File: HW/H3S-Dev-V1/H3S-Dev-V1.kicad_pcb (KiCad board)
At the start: 2 copper layers, 85 x 56 mm, 33 parts, among them J1 USB_C_Receptacle_USB2.0_16P, J2 Conn_01x02_Socket, J3 Conn_Coaxial, Q1 DMP3099L, U1 Ai-Thinker-Ra-01, U2 LTC4054ES5-4.2, U3 USBLC6-2SC6, U4 ESP32-S3-WROOM-1, U5 SY8089AAAC

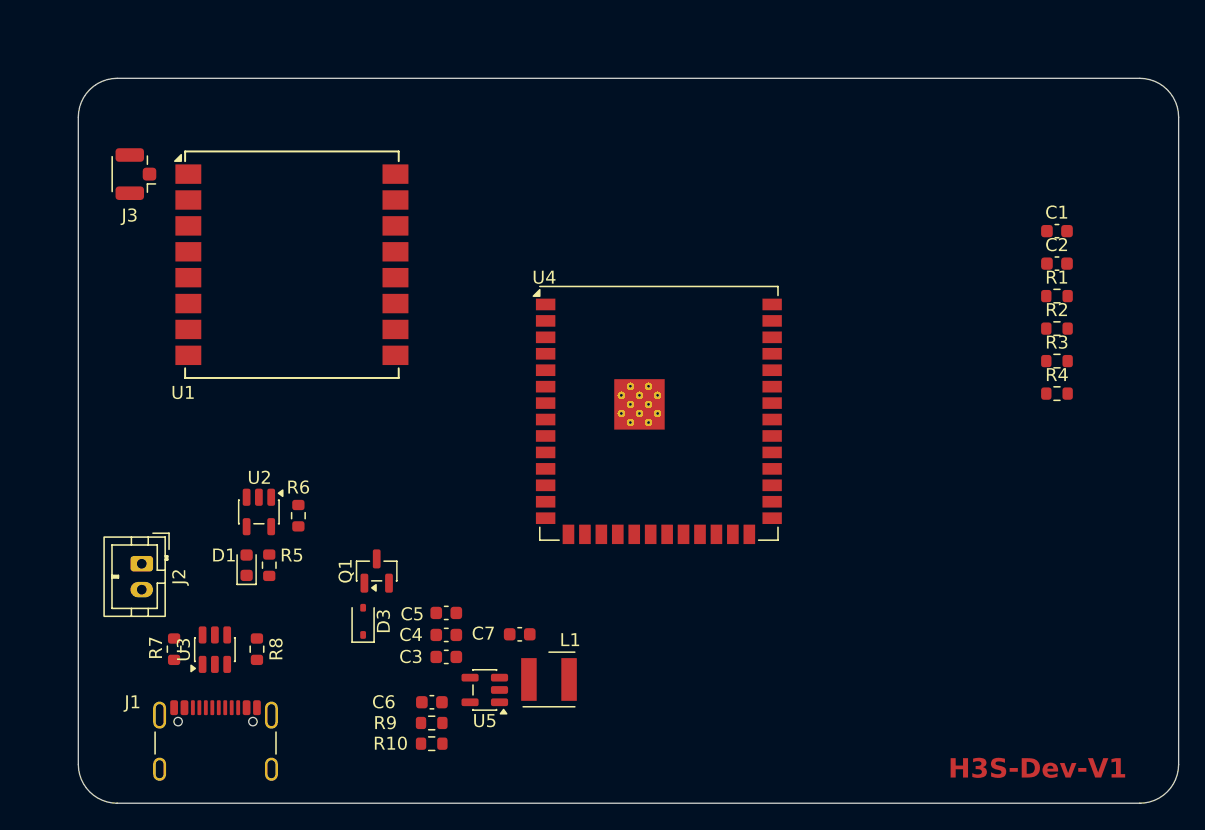
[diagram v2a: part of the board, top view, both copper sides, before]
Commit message: PCB dimensions
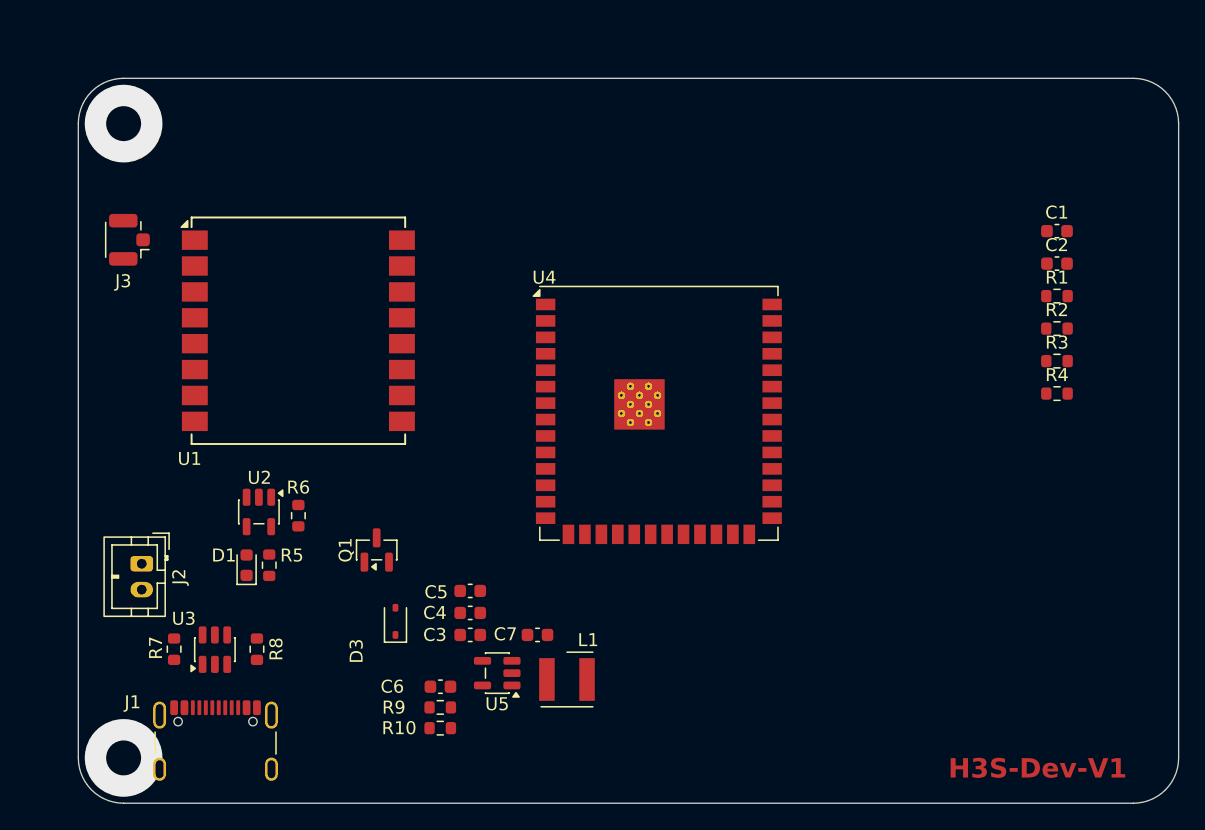
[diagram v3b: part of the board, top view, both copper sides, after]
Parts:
- moved U1 5.12 mm to (117.0, 93.5)
- moved J3 5.10 mm to (104.0, 86.5)
- moved C3 2.51 mm to (130.3, 117.0)
- moved C4 2.51 mm to (130.3, 115.3)
- moved C5 2.51 mm to (130.3, 113.6)
- moved D3 2.50 mm to (124.5, 116.0)
- moved Q1 1.62 mm to (123.0, 110.4)
- moved U5 1.62 mm to (132.4, 120.0)
- moved L1 1.39 mm to (137.8, 120.4)
- moved C7 1.38 mm to (135.5, 117.0)
- moved C6 1.37 mm to (128.0, 121.0)
- moved R10 1.37 mm to (128.0, 124.2)
- moved R9 1.37 mm to (128.0, 122.6)
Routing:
- net GND: vias 0 -> 2
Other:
- outline, holes or cut-outs redrawn
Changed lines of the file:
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@@
 	(footprint "Connector_Coaxial:U.FL_Hirose_U.FL-R-SMT-1_Vertical"
 		(layer "F.Cu")
-		(at 104.45 81.4 180)
+		(at 103.95 86.475 180)
 		(descr "Hirose U.FL Coaxial https://www.hirose.com/product/en/products/U.FL/U.FL-R-SMT-1%2810%29/")
 		(tags "Hirose U.FL Coaxial")
@@
 			(polygon
 				(pts
-					(xy 102.875 82.35) (xy 104.965 82.35) (xy 104.965 80.45) (xy 102.875 80.45)
+					(xy 102.375 87.425) (xy 104.465 87.425) (xy 104.465 85.525) (xy 102.375 85.525)
 				)
 			)
@@
 	(footprint "Capacitor_SMD:C_0603_1608Metric"
 		(layer "F.Cu")
-		(at 127.315 122.2)
+		(at 127.975 121)
 		(descr "Capacitor SMD 0603 (1608 Metric), square (rectangular) end terminal, IPC-7351 nominal, (Body size source: IPC-SM-782 page 76, https://www.pcb-3d.com/wordpress/wp-content/uploads/ipc-sm-782a_amendment_1_and_2.pdf), generated with kicad-footprint-generator")
 		(tags "capacitor")
@@
 	(footprint "Resistor_SMD:R_0603_1608Metric"
 		(layer "F.Cu")
-		(at 127.3 123.8)
+		(at 127.96 122.6)
 		(descr "Resistor SMD 0603 (1608 Metric), square (rectangular) end terminal, IPC-7351 nominal, (Body size source: IPC-SM-782 page 72, https://www.pcb-3d.com/wordpress/wp-content/uploads/ipc-sm-782a_amendment_1_and_2.pdf), generated with kicad-footprint-generator")
 		(tags "resistor")
@@
 	(footprint "Package_TO_SOT_SMD:SOT-23"
 		(layer "F.Cu")
-		(at 123.05 112.0625 90)
+		(at 123.05 110.4375 90)
 		(descr "SOT, 3 Pin (JEDEC TO-236 Var AB https://www.jedec.org/document_search?search_api_views_fulltext=TO-236), generated with kicad-footprint-generator ipc_gullwing_generator.py")
 		(tags "SOT TO_SOT_SMD")
@@
 	(footprint "Capacitor_SMD:C_0603_1608Metric"
 		(layer "F.Cu")
-		(at 128.425 115.3)
+		(at 130.275 113.6)
 		(descr "Capacitor SMD 0603 (1608 Metric), square (rectangular) end terminal, IPC-7351 nominal, (Body size source: IPC-SM-782 page 76, https://www.pcb-3d.com/wordpress/wp-content/uploads/ipc-sm-782a_amendment_1_and_2.pdf), generated with kicad-footprint-generator")
 		(tags "capacitor")
@@
 	(footprint "Inductor_SMD_Wurth:L_Wurth_WE-LQSH-4020"
 		(layer "F.Cu")
-		(at 136.36 120.44)
+		(at 137.75 120.44)
 		(descr "Semi-Shielded High Saturation Power Inductor, body 4x4mm, https://www.we-online.com/catalog/en/WE-LQSH#/articles/WE-LQSH-4020")
 		(tags "SMT")
@@
 	(footprint "Package_TO_SOT_SMD:SOT-23-5"
 		(layer "F.Cu")
-		(at 131.4 121.25 180)
+		(at 132.3625 119.95 180)
 		(descr "SOT, 5 Pin (JEDEC MO-178 Var AA https://www.jedec.org/document_search?search_api_views_fulltext=MO-178), generated with kicad-footprint-generator ipc_gullwing_generator.py")
 		(tags "SOT TO_SOT_SMD")
@@
 	(footprint "Diode_SMD:D_SOD-323"
 		(layer "F.Cu")
-		(at 122 115.95 90)
+		(at 124.5 115.95 90)
 		(descr "SOD-323")
 		(tags "SOD-323")
 		(property "Reference" "D3"
-			(at 0 1.6 90)
+			(at -2.3 -3 90)
 			(layer "F.SilkS")
 			(effects
@@
 		)
 		(fp_text user "${REFERENCE}"
-			(at 0 -1.85 90)
+			(at 0 -1.75 90)
 			(layer "F.Fab")
 			(effects
@@
 	(footprint "Capacitor_SMD:C_0603_1608Metric"
 		(layer "F.Cu")
-		(at 128.425 118.7)
+		(at 130.275 117)
 		(descr "Capacitor SMD 0603 (1608 Metric), square (rectangular) end terminal, IPC-7351 nominal, (Body size source: IPC-SM-782 page 76, https://www.pcb-3d.com/wordpress/wp-content/uploads/ipc-sm-782a_amendment_1_and_2.pdf), generated with kicad-footprint-generator")
 		(tags "capacitor")
@@
 	(footprint "RF_Module:Ai-Thinker-Ra-01-LoRa"
 		(layer "F.Cu")
-		(at 116.5 88.4)
+		(at 117 93.5)
 		(descr "Ai Thinker Ra-01 LoRa")
 		(tags "LoRa Ra-01")
@@
 	(footprint "Capacitor_SMD:C_0603_1608Metric"
 		(layer "F.Cu")
-		(at 134.1 116.95 180)
+		(at 135.475 117 180)
 		(descr "Capacitor SMD 0603 (1608 Metric), square (rectangular) end terminal, IPC-7351 nominal, (Body size source: IPC-SM-782 page 76, https://www.pcb-3d.com/wordpress/wp-content/uploads/ipc-sm-782a_amendment_1_and_2.pdf), generated with kicad-footprint-generator")
 		(tags "capacitor")
 		(property "Reference" "C7"
-			(at 2.8 0.05 0)
+			(at 2.475 0.05 0)
 			(layer "F.SilkS")
 			(effects
@@
 		(tags "SOT TO_SOT_SMD")
 		(property "Reference" "U3"
-			(at 0 -2.4 90)
+			(at 2.3875 -2.4 180)
 			(layer "F.SilkS")
 			(effects
@@
 	(footprint "Capacitor_SMD:C_0603_1608Metric"
 		(layer "F.Cu")
-		(at 128.425 117)
+		(at 130.275 115.3)
 		(descr "Capacitor SMD 0603 (1608 Metric), square (rectangular) end terminal, IPC-7351 nominal, (Body size source: IPC-SM-782 page 76, https://www.pcb-3d.com/wordpress/wp-content/uploads/ipc-sm-782a_amendment_1_and_2.pdf), generated with kicad-footprint-generator")
 		(tags "capacitor")
@@
 	(footprint "Resistor_SMD:R_0603_1608Metric"
 		(layer "F.Cu")
-		(at 127.3 125.4 180)
+		(at 127.96 124.2 180)
 		(descr "Resistor SMD 0603 (1608 Metric), square (rectangular) end terminal, IPC-7351 nominal, (Body size source: IPC-SM-782 page 72, https://www.pcb-3d.com/wordpress/wp-content/uploads/ipc-sm-782a_amendment_1_and_2.pdf), generated with kicad-footprint-generator")
 		(tags "resistor")
@@
 	)
 	(gr_arc
-		(start 103 130)
-		(mid 100.87868 129.12132)
-		(end 100 127)
+		(start 100 77.5)
+		(mid 101.025126 75.025126)
+		(end 103.5 74)
 		(stroke
-			(width 0.05)
-			(type default)
+			(width 0.1)
+			(type solid)
 		)
 		(locked yes)
 		(layer "Edge.Cuts")
 	)
-	(gr_arc
-		(start 185 127)
-		(mid 184.12132 129.12132)
-		(end 182 130)
+	(gr_line
+		(start 181.5 74)
+		(end 103.5 74)
 		(stroke
-			(width 0.05)
-			(type default)
+			(width 0.1)
+			(type solid)
 		)
 		(locked yes)
@@
 	)
 	(gr_line
-		(start 185 77)
-		(end 185 127)
+		(start 103.5 130)
+		(end 181.5 130)
 		(stroke
-			(width 0.05)
-			(type default)
+			(width 0.1)
+			(type solid)
 		)
 		(locked yes)
 		(layer "Edge.Cuts")
 	)
-	(gr_line
-		(start 103 130)
-		(end 182 130)
+	(gr_arc
+		(start 103.5 130)
+		(mid 101.025126 128.974874)
+		(end 100 126.5)
 		(stroke
-			(width 0.05)
-			(type default)
+			(width 0.1)
+			(type solid)
 		)
 		(locked yes)
 		(layer "Edge.Cuts")
 	)
-	(gr_arc
-		(start 182 74)
-		(mid 184.12132 74.87868)
-		(end 185 77)
+	(gr_line
+		(start 100 77.5)
+		(end 100 126.5)
 		(stroke
-			(width 0.05)
-			(type default)
+			(width 0.1)
+			(type solid)
 		)
 		(locked yes)
 		(layer "Edge.Cuts")
 	)
-	(gr_line
-		(start 100 77)
-		(end 100 127)
+	(gr_arc
+		(start 185 126.5)
+		(mid 183.974874 128.974874)
+		(end 181.5 130)
 		(stroke
-			(width 0.05)
-			(type default)
+			(width 0.1)
+			(type solid)
 		)
 		(locked yes)
@@
 	)
 	(gr_line
-		(start 103 74)
-		(end 182 74)
+		(start 185 126.5)
+		(end 185 77.5)
 		(stroke
-			(width 0.05)
-			(type default)
+			(width 0.1)
+			(type solid)
 		)
 		(locked yes)
@@
 	)
 	(gr_arc
-		(start 100 77)
-		(mid 100.87868 74.87868)
-		(end 103 74)
+		(start 181.5 74)
+		(mid 183.974874 75.025126)
+		(end 185 77.5)
 		(stroke
-			(width 0.05)
-			(type default)
+			(width 0.1)
+			(type solid)
 		)
 		(locked yes)
 		(layer "Edge.Cuts")
 	)
-	(gr_arc
-		(start 185 127)
-		(mid 184.12132 129.12132)
-		(end 182 130)
+	(gr_line
+		(start 100.000001 126.5)
+		(end 100.000001 77.499999)
 		(stroke
-			(width 0.5)
+			(width 1)
 			(type solid)
 		)
@@
 		(layer "Margin")
 	)
-	(gr_line
-		(start 103 130)
-		(end 182 130)
+	(gr_arc
+		(start 100.000001 77.5)
+		(mid 101.025127 75.025126)
+		(end 103.500001 74)
 		(stroke
-			(width 0.5)
+			(width 1)
 			(type solid)
 		)
@@
 		(layer "Margin")
 	)
-	(gr_line
-		(start 100 77)
-		(end 100 127)
+	(gr_arc
+		(start 103.5 130)
+		(mid 101.025126 128.974874)
+		(end 100 126.5)
 		(stroke
-			(width 0.5)
+			(width 1)
 			(type solid)
 		)
@@
 	)
 	(gr_arc
-		(start 100 77)
-		(mid 100.87868 74.87868)
-		(end 103 74)
+		(start 181.500001 74.000001)
+		(mid 183.974875 75.025127)
+		(end 185.000001 77.500001)
 		(stroke
-			(width 0.5)
+			(width 1)
 			(type solid)
 		)
@@
 	)
 	(gr_line
-		(start 103 74)
-		(end 182 74)
+		(start 103.5 130)
+		(end 181.5 130)
 		(stroke
-			(width 0.5)
+			(width 1)
 			(type solid)
 		)
@@
 		(layer "Margin")
 	)
-	(gr_arc
-		(start 103 130)
-		(mid 100.87868 129.12132)
-		(end 100 127)
+	(gr_line
+		(start 184.999999 126.500002)
+		(end 184.999999 77.500001)
 		(stroke
-			(width 0.5)
+			(width 1)
 			(type solid)
 		)
@@
 	)
 	(gr_arc
-		(start 182 74)
-		(mid 184.12132 74.87868)
-		(end 185 77)
+		(start 184.999999 126.499999)
+		(mid 183.974873 128.974873)
+		(end 181.499999 129.999999)
 		(stroke
-			(width 0.5)
+			(width 1)
 			(type solid)
 		)
@@
 	)
 	(gr_line
-		(start 185 77)
-		(end 185 127)
+		(start 103.5 74)
+		(end 181.5 74)
 		(stroke
-			(width 0.5)
+			(width 1)
 			(type solid)
 		)
@@
 		)
 	)
+	(via
+		(at 103.5 126.5)
+		(size 6)
+		(drill 2.7)
+		(layers "F.Cu" "B.Cu")
+		(net 2)
+	)
+	(via
+		(at 103.5 77.5)
+		(size 6)
+		(drill 2.7)
+		(layers "F.Cu" "B.Cu")
+		(net 2)
+	)
 	(embedded_fonts no)

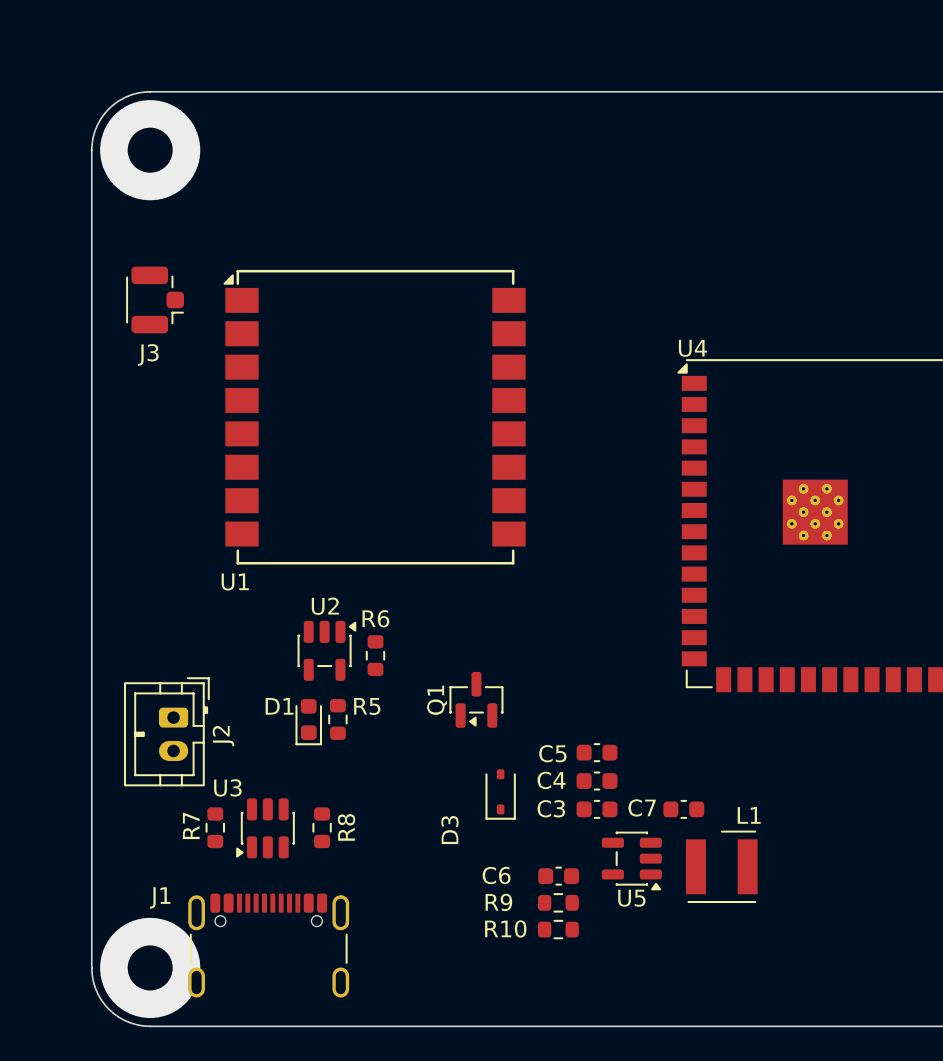
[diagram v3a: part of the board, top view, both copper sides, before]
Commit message: dc-dc routing
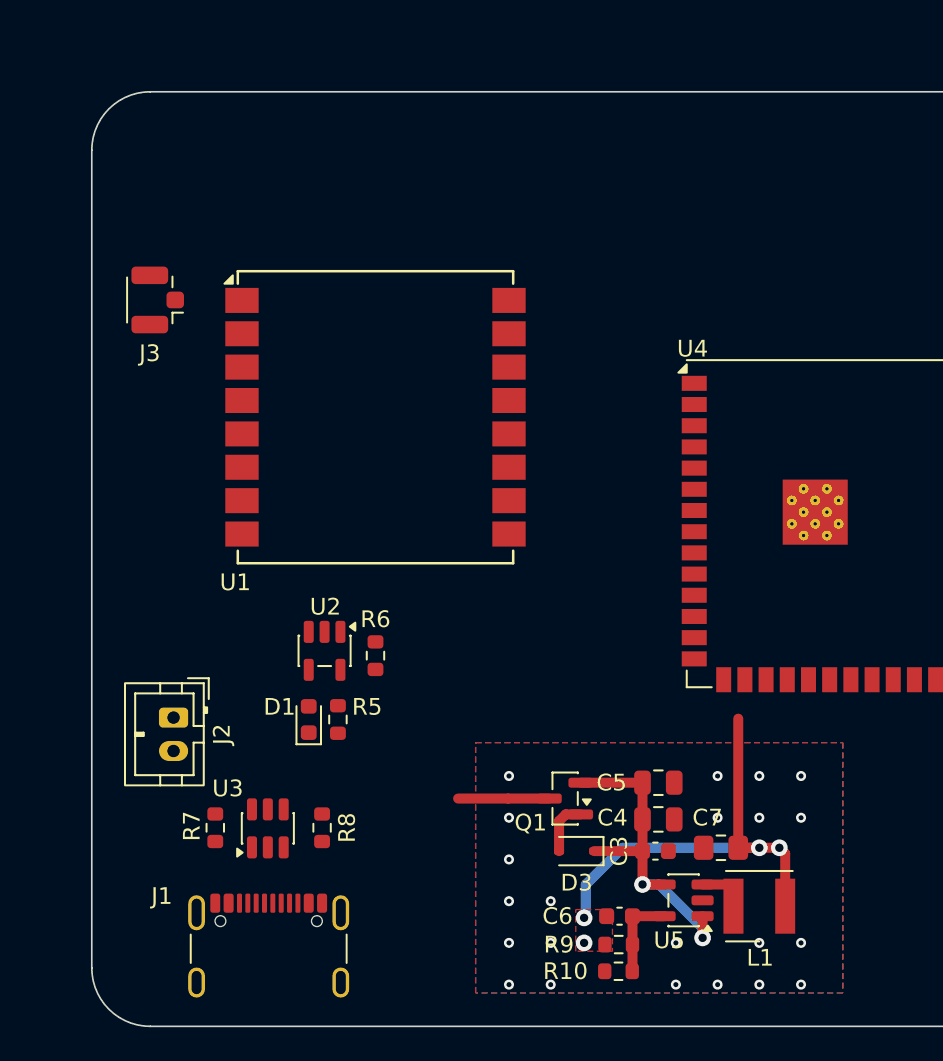
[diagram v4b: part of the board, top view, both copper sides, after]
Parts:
- C4, C5: footprint Capacitor_SMD:C_0603_1608Metric -> Capacitor_SMD:C_0805_2012Metric
- C7: footprint Capacitor_SMD:C_0603_1608Metric -> Capacitor_SMD:C_0805_2012Metric_Pad1.18x1.45mm_HandSolder
- moved Q1 7.95 mm to (128.4, 116.3), turned to 180 degrees
- moved D3 5.77 mm to (129.1, 119.5), turned to 180 degrees
- moved R9 4.40 mm to (131.6, 125.1)
- moved R10 4.38 mm to (131.6, 126.7)
- moved C6 4.37 mm to (131.6, 123.4)
- moved C4 4.34 mm to (133.9, 117.6)
- moved C3 4.30 mm to (133.8, 119.5)
- moved C5 4.09 mm to (133.9, 115.4)
- moved U5 3.98 mm to (135.5, 122.5)
- moved L1 3.26 mm to (140.0, 122.8), turned to 180 degrees
- moved C7 3.20 mm to (137.7, 119.3)
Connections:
- L1 pad 1: Net-(U5-LX) -> VCC
- L1 pad 2: VCC -> Net-(U5-LX)
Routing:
- net VCC: track 0.00 -> 27.2 mm, vias 0 -> 4
- net Net-(D3-K): track 0.00 -> 20.6 mm, vias 0 -> 2
- net /VBAT: track 0.00 -> 5.47 mm
- net Net-(U5-FB): track 0.00 -> 5.23 mm
- net /VBUS: track 0.00 -> 3.27 mm
- net Net-(U5-LX): track 0.00 -> 3.00 mm
- net GND: vias 2 -> 22
- added copper zone on B.Cu, net GND
- added copper zone on F.Cu, net GND
- added copper zone on F.Cu, net VCC
